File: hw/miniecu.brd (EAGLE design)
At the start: 50 x 50 mm, 60 parts

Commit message: pcb: gerbers for IDTEAD Studio
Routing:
- net AGND: track 10.4 -> 12.4 mm
- net GND: track 93.8 -> 94.8 mm
- net +3V3: track 153.8 -> 153.1 mm
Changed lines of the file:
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@@
 <element name="XP2" library="miniecu-con" package="B3B-XH" value="FLOW_SENS-B3B-XH-A" x="46" y="15" smashed="yes" rot="R90">
 <attribute name="NAME" x="41.5" y="18" size="1.27" layer="21" font="vector" rot="R90"/>
-<attribute name="VALUE" x="54.31" y="7.96" size="1.27" layer="21" rot="R90"/>
 </element>
 <element name="XP4" library="miniecu-con" package="B4B-XH" value="IGN_POWER-B4B-XH-A" x="4" y="16" smashed="yes" rot="R270">
 <attribute name="NAME" x="8.31" y="23.31" size="1.27" layer="21" font="vector" rot="R270"/>
-<attribute name="VALUE" x="-4.81" y="22.81" size="1.27" layer="21" rot="R270"/>
 </element>
 <element name="XP1" library="miniecu-con" package="B6B-XH" value="SENSORS-B6B-XH-A" x="4" y="32" smashed="yes" rot="R270">
 <attribute name="NAME" x="7.81" y="43.85" size="1.27" layer="21" font="vector" rot="R270"/>
-<attribute name="VALUE" x="-4.81" y="41.35" size="1.27" layer="21" rot="R270"/>
 </element>
 <element name="XP3" library="miniecu-con" package="B4B-XH" value="UART-B4B-XH-A" x="46" y="34" smashed="yes" rot="R90">
 <attribute name="NAME" x="41.5" y="27" size="1.27" layer="21" font="vector" rot="R90"/>
-<attribute name="VALUE" x="54.31" y="29.69" size="1.27" layer="21" rot="R90"/>
 </element>
 <element name="C15" library="resistor" package="C0603" value="0.1" x="40.5" y="38" smashed="yes" rot="R180">
@@
 <wire x1="27.5" y1="30" x2="27.5" y2="30.635" width="0.5" layer="16"/>
 <wire x1="27.5" y1="30.635" x2="27.135" y2="31" width="0.5" layer="16"/>
+<wire x1="27.5" y1="31" x2="27.5" y2="32" width="0.8" layer="16"/>
+<wire x1="27.135" y1="31" x2="27.5" y2="31" width="0" layer="19" extent="16-16"/>
 </signal>
 <signal name="VBAT">
@@
 <vertex x="2" y="40.5"/>
 <vertex x="2.5" y="41"/>
-<vertex x="19.5" y="41"/>
-<vertex x="26" y="35"/>
+<vertex x="18.5" y="41"/>
+<vertex x="26" y="34"/>
 <vertex x="26" y="26.5"/>
 <vertex x="24.5" y="25"/>
@@
 <wire x1="15.7" y1="36" x2="13" y2="36" width="0.5" layer="1"/>
 <via x="13" y="36" extent="1-16" drill="0.6"/>
-<wire x1="15.7" y1="36" x2="25.865" y2="31" width="0" layer="19" extent="1-16"/>
+<wire x1="25.5" y1="30" x2="25.5" y2="32" width="0.8" layer="16"/>
+<wire x1="25.5" y1="30" x2="25.865" y2="31" width="0" layer="19" extent="16-16"/>
+<wire x1="15.7" y1="36" x2="25.5" y2="32" width="0" layer="19" extent="1-16"/>
 </signal>
 <signal name="+3V3">
@@
 <wire x1="33.5" y1="17.5" x2="34" y2="18" width="0.8" layer="1"/>
 <wire x1="34" y1="18" x2="40.5" y2="18" width="0.8" layer="1"/>
-<wire x1="19.85" y1="41" x2="19.85" y2="42.35" width="0.8" layer="1"/>
-<wire x1="19.85" y1="42.35" x2="20" y2="42.5" width="0.8" layer="1"/>
-<via x="20" y="42.5" extent="1-16" drill="0.6"/>
-<wire x1="20" y1="42.5" x2="32" y2="42.5" width="0.8" layer="16"/>
+<wire x1="19.85" y1="41" x2="19.85" y2="41.85" width="0.8" layer="1"/>
+<wire x1="19.85" y1="41.85" x2="20.5" y2="42.5" width="0.8" layer="1"/>
+<via x="20.5" y="42.5" extent="1-16" drill="0.6"/>
+<wire x1="20.5" y1="42.5" x2="32" y2="42.5" width="0.8" layer="16"/>
 <wire x1="32" y1="42.5" x2="33.5" y2="41" width="0.8" layer="16"/>
-<wire x1="20" y1="42.5" x2="22" y2="42.5" width="0.8" layer="16"/>
+<wire x1="20.5" y1="42.5" x2="22" y2="42.5" width="0.8" layer="16"/>
 <wire x1="22" y1="42.5" x2="22.5" y2="43" width="0.8" layer="16"/>
 <via x="22.5" y="43" extent="1-16" drill="0.6"/>

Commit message: sch: change LDO MCP1700 (6V max) -> MCP1703 (16V max) in the same package
Fix LDO ceramic capasitance from 4.7 µF to 1.0 µF (MCP1703 DS)
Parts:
- C6, C8: value 4.7 -> 1.0
- DA1: value (none) -> MCP1703
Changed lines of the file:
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@@
 <attribute name="VALUE" x="30.032" y="46.111" size="1.27" layer="27" rot="R90"/>
 </element>
-<element name="DA1" library="power-ic" package="SOT23" value="" x="20" y="16" smashed="yes">
+<element name="DA1" library="power-ic" package="SOT23" value="MCP1703" x="20" y="16" smashed="yes">
 <attribute name="NAME" x="23.095" y="15.095" size="1.27" layer="25" font="vector" rot="R90"/>
 <attribute name="VALUE" x="18.095" y="12.825" size="1.27" layer="27"/>
@@
 <attribute name="VALUE" x="13.857" y="17.016" size="0.4064" layer="27" font="vector" rot="R270"/>
 </element>
-<element name="C6" library="resistor" package="C0805" value="4.7" x="17" y="16" smashed="yes" rot="R270">
+<element name="C6" library="resistor" package="C0805" value="1.0" x="17" y="16" smashed="yes" rot="R270">
 <attribute name="NAME" x="17.5" y="12.5" size="1.27" layer="25" font="vector" rot="R90"/>
 <attribute name="VALUE" x="14.714" y="16.889" size="1.27" layer="27" rot="R270"/>
 </element>
-<element name="C8" library="resistor" package="C0805" value="4.7" x="20" y="13" smashed="yes" rot="R180">
+<element name="C8" library="resistor" package="C0805" value="1.0" x="20" y="13" smashed="yes" rot="R180">
 <attribute name="NAME" x="21" y="12" size="1.27" layer="25" font="vector" rot="R180"/>
 <attribute name="VALUE" x="20.889" y="15.286" size="1.27" layer="27" rot="R180"/>

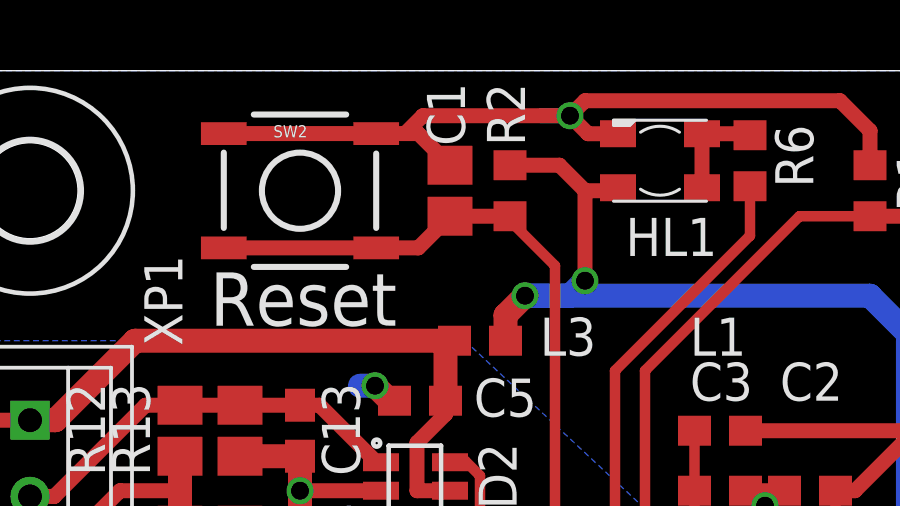
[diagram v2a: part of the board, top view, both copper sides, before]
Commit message: sch: minimize BOM (by resistor values)
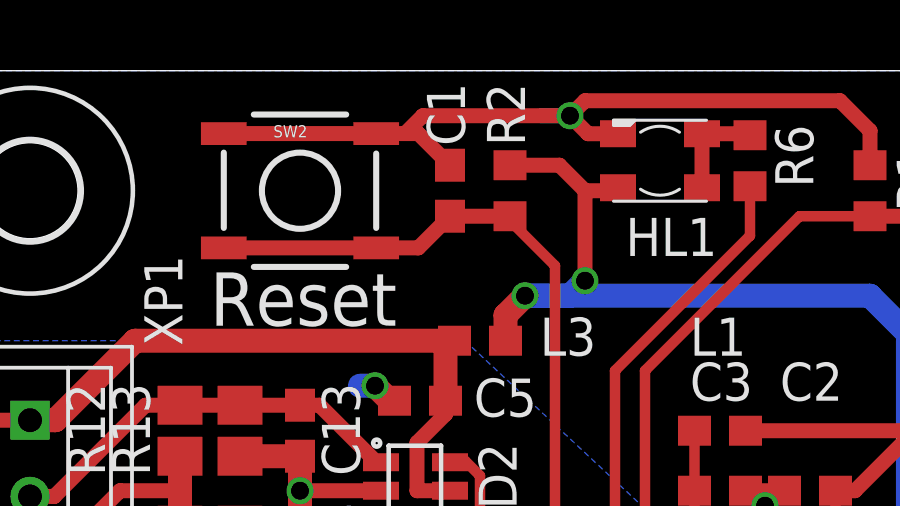
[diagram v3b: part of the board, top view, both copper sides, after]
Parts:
- C1: device resistor:C0805 -> resistor:C0603
- R1, R2, R9: value 10k -> 5.1k
- R12, R16, R19, R3, R4, R5, R7: value 10k -> 10k 1%
- R14, R15, R8: value 100 -> 140
- XP1: value SENSORS-B6B-XH-A -> B6B-XH-A
- XP2: value FLOW_SENS-B3B-XH-A -> B3B-XH-A
- XP3: value UART-B4B-XH-A -> B4B-XH-A
- XP4: value IGN_POWER-B4B-XH-A -> B4B-XH-A
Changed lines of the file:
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@@
 <attribute name="VALUE" x="36.095" y="29.555" size="1.27" layer="27"/>
 </element>
-<element name="XP2" library="miniecu-con" package="B3B-XH" value="FLOW_SENS-B3B-XH-A" x="46" y="15" smashed="yes" rot="R90">
+<element name="XP2" library="miniecu-con" package="B3B-XH" value="B3B-XH-A" x="46" y="15" smashed="yes" rot="R90">
 <attribute name="NAME" x="41.5" y="18" size="1.27" layer="21" font="vector" rot="R90"/>
 </element>
-<element name="XP4" library="miniecu-con" package="B4B-XH" value="IGN_POWER-B4B-XH-A" x="4" y="16" smashed="yes" rot="R270">
+<element name="XP4" library="miniecu-con" package="B4B-XH" value="B4B-XH-A" x="4" y="16" smashed="yes" rot="R270">
 <attribute name="NAME" x="8.31" y="23.31" size="1.27" layer="21" font="vector" rot="R270"/>
 </element>
-<element name="XP1" library="miniecu-con" package="B6B-XH" value="SENSORS-B6B-XH-A" x="4" y="32" smashed="yes" rot="R270">
+<element name="XP1" library="miniecu-con" package="B6B-XH" value="B6B-XH-A" x="4" y="32" smashed="yes" rot="R270">
 <attribute name="NAME" x="7.81" y="43.85" size="1.27" layer="21" font="vector" rot="R270"/>
 </element>
-<element name="XP3" library="miniecu-con" package="B4B-XH" value="UART-B4B-XH-A" x="46" y="34" smashed="yes" rot="R90">
+<element name="XP3" library="miniecu-con" package="B4B-XH" value="B4B-XH-A" x="46" y="34" smashed="yes" rot="R90">
 <attribute name="NAME" x="41.5" y="27" size="1.27" layer="21" font="vector" rot="R90"/>
 </element>
@@
 <attribute name="VALUE" x="10.968" y="26.889" size="1.27" layer="27" rot="R270"/>
 </element>
-<element name="R14" library="resistor" package="R0603" value="100" x="10" y="30" smashed="yes" rot="R270">
+<element name="R14" library="resistor" package="R0603" value="140" x="10" y="30" smashed="yes" rot="R270">
 <attribute name="NAME" x="7.5" y="28.5" size="1.27" layer="25" font="vector" rot="R90"/>
 <attribute name="VALUE" x="7.968" y="30.889" size="1.27" layer="27" rot="R270"/>
@@
 <attribute name="VALUE" x="11.968" y="30.889" size="1.27" layer="27" rot="R270"/>
 </element>
-<element name="R16" library="resistor" package="R0805" value="10k" x="9" y="34" smashed="yes" rot="R90">
+<element name="R16" library="resistor" package="R0805" value="10k 1%" x="9" y="34" smashed="yes" rot="R90">
 <attribute name="NAME" x="6.5" y="32.5" size="1.27" layer="25" font="vector" rot="R90"/>
 <attribute name="VALUE" x="11.286" y="33.238" size="1.27" layer="27" rot="R90"/>
 </element>
-<element name="R12" library="resistor" package="R0805" value="10k" x="9" y="38" smashed="yes" rot="R270">
+<element name="R12" library="resistor" package="R0805" value="10k 1%" x="9" y="38" smashed="yes" rot="R270">
 <attribute name="NAME" x="6.5" y="36.5" size="1.27" layer="25" font="vector" rot="R90"/>
 <attribute name="VALUE" x="6.714" y="38.762" size="1.27" layer="27" rot="R270"/>
@@
 <attribute name="VALUE" x="10.968" y="38.889" size="1.27" layer="27" rot="R270"/>
 </element>
-<element name="R15" library="resistor" package="R0603" value="100" x="40" y="12" smashed="yes">
+<element name="R15" library="resistor" package="R0603" value="140" x="40" y="12" smashed="yes">
 <attribute name="NAME" x="38.611" y="9.889" size="1.27" layer="25" font="vector"/>
 <attribute name="VALUE" x="39.111" y="9.968" size="1.27" layer="27"/>
@@
 <attribute name="VALUE" x="17.889" y="41.032" size="1.27" layer="27" rot="R180"/>
 </element>
-<element name="C1" library="resistor" package="C0805" value="0.022" x="18" y="46" smashed="yes" rot="R90">
+<element name="C1" library="resistor" package="C0603" value="0.022" x="18" y="46" smashed="yes" rot="R90">
 <attribute name="NAME" x="18.5" y="47.5" size="1.27" layer="25" font="vector" rot="R90"/>
 <attribute name="VALUE" x="20.286" y="45.111" size="1.27" layer="27" rot="R90"/>
@@
 <attribute name="VALUE" x="20.889" y="15.286" size="1.27" layer="27" rot="R180"/>
 </element>
-<element name="R4" library="resistor" package="R0805" value="10k" x="20" y="21.5" smashed="yes">
+<element name="R4" library="resistor" package="R0805" value="10k 1%" x="20" y="21.5" smashed="yes">
 <attribute name="NAME" x="19.238" y="22.516" size="1.27" layer="25" font="vector"/>
 <attribute name="VALUE" x="19.238" y="19.214" size="1.27" layer="27"/>
 </element>
-<element name="R5" library="resistor" package="R0805" value="10k" x="16" y="19.5" smashed="yes">
+<element name="R5" library="resistor" package="R0805" value="10k 1%" x="16" y="19.5" smashed="yes">
 <attribute name="NAME" x="14" y="22" size="1.27" layer="25" font="vector" rot="R90"/>
 <attribute name="VALUE" x="15.238" y="17.214" size="1.27" layer="27"/>
@@
 <attribute name="NAME" x="7.8" y="14.3" size="1.27" layer="25" font="vector" rot="R90"/>
 </element>
-<element name="R8" library="resistor" package="R0603" value="100" x="9.5" y="9.5" smashed="yes" rot="R90">
+<element name="R8" library="resistor" package="R0603" value="140" x="9.5" y="9.5" smashed="yes" rot="R90">
 <attribute name="NAME" x="7.5" y="11" size="1.27" layer="25" font="vector" rot="R270"/>
 <attribute name="VALUE" x="11.532" y="8.611" size="1.27" layer="27" rot="R90"/>
 </element>
-<element name="R9" library="resistor" package="R0603" value="10k" x="15.5" y="9.5" smashed="yes" rot="R90">
+<element name="R9" library="resistor" package="R0603" value="5.1k" x="15.5" y="9.5" smashed="yes" rot="R90">
 <attribute name="NAME" x="17.5" y="8.5" size="1.27" layer="25" font="vector" rot="R90"/>
 <attribute name="VALUE" x="17.532" y="8.611" size="1.27" layer="27" rot="R90"/>
 </element>
-<element name="R7" library="resistor" package="R0805" value="10k" x="11.5" y="9.5" smashed="yes" rot="R270">
+<element name="R7" library="resistor" package="R0805" value="10k 1%" x="11.5" y="9.5" smashed="yes" rot="R270">
 <attribute name="NAME" x="10.5" y="11" size="1.27" layer="25" font="vector"/>
 <attribute name="VALUE" x="9.214" y="10.262" size="1.27" layer="27" rot="R270"/>
@@
 <attribute name="VALUE" x="11.468" y="10.389" size="1.27" layer="27" rot="R270"/>
 </element>
-<element name="R19" library="resistor" package="R0805" value="10k" x="41" y="15" smashed="yes" rot="R90">
+<element name="R19" library="resistor" package="R0805" value="10k 1%" x="41" y="15" smashed="yes" rot="R90">
 <attribute name="NAME" x="39.5" y="17" size="1.27" layer="25" font="vector" rot="R90"/>
 <attribute name="VALUE" x="43.286" y="14.238" size="1.27" layer="27" rot="R90"/>
@@
 <element name="H3" library="holes" package="3,2" value="MOUNT-HOLE3.2" x="4" y="46"/>
 <element name="H4" library="holes" package="3,2" value="MOUNT-HOLE3.2" x="46" y="46"/>
-<element name="R1" library="resistor" package="R0603" value="10k" x="32" y="46" smashed="yes" rot="R270">
+<element name="R1" library="resistor" package="R0603" value="5.1k" x="32" y="46" smashed="yes" rot="R270">
 <attribute name="NAME" x="32.889" y="47.389" size="1.27" layer="25" font="vector" rot="R270"/>
 <attribute name="VALUE" x="29.968" y="46.889" size="1.27" layer="27" rot="R270"/>
 </element>
-<element name="R2" library="resistor" package="R0603" value="10k" x="20" y="46" smashed="yes" rot="R90">
+<element name="R2" library="resistor" package="R0603" value="5.1k" x="20" y="46" smashed="yes" rot="R90">
 <attribute name="NAME" x="20.5" y="47.5" size="1.27" layer="25" font="vector" rot="R90"/>
 <attribute name="VALUE" x="22.032" y="45.111" size="1.27" layer="27" rot="R90"/>
 </element>
-<element name="R3" library="resistor" package="R0805" value="10k" x="20" y="19.5" smashed="yes" rot="R180">
+<element name="R3" library="resistor" package="R0805" value="10k 1%" x="20" y="19.5" smashed="yes" rot="R180">
 <attribute name="NAME" x="20.762" y="18.484" size="1.27" layer="25" font="vector" rot="R180"/>
 <attribute name="VALUE" x="20.762" y="21.786" size="1.27" layer="27" rot="R180"/>

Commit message: hw: release hw v1b, update gerbers
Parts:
- renumbered U$1 to LOGO2
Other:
- board text added: "2014 rev.1b"
- board text added: "miniECU rev.1b engine monitoring with kill switch"
- board text removed: "2014 rev 1"
- board text removed: "miniECU v1 engine monitoring with kill switch"
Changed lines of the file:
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@@
 </polygon>
 <text x="33" y="2.5" size="1.778" layer="21" font="vector">2014
-rev 1</text>
+rev.1b</text>
 <text x="42.5" y="25" size="1.778" layer="21" font="vector">UART</text>
 <text x="42.5" y="21" size="1.778" layer="21" font="vector">FLOW</text>
@@
 <text x="35" y="31.75" size="2" layer="22" font="vector" rot="MR0" align="bottom-right">TXD</text>
 <text x="35" y="29.25" size="2" layer="22" font="vector" rot="MR0" align="bottom-right">VCCi</text>
-<text x="10.5" y="9.5" size="2" layer="22" font="fixed" rot="MR180">miniECU v1
+<text x="10.5" y="9.5" size="2" layer="22" font="fixed" rot="MR180">miniECU rev.1b
 engine monitoring
 with kill switch</text>
@@
 </element>
 <element name="LOGO1" library="SparkFun-Aesthetics" package="OSHW-LOGO-L" value="OSHW-LOGOL" x="28" y="12"/>
-<element name="U$1" library="miniecu" package="MINIECU_LOGO" value="MINIECU_LOGO" x="11" y="2"/>
+<element name="LOGO2" library="miniecu" package="MINIECU_LOGO" value="MINIECU_LOGO" x="11" y="2"/>
 </elements>
 <signals>
